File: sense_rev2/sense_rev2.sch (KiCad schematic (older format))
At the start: 48 parts, among them P1 TST, P2 TST, P3 TST, P4 TST, Q1 TSM2301, U1 PIR, U2 TLV8801, U3 TLV8801, U4 TPS61098, U5 hackaBLE_half, U6 TPS70630

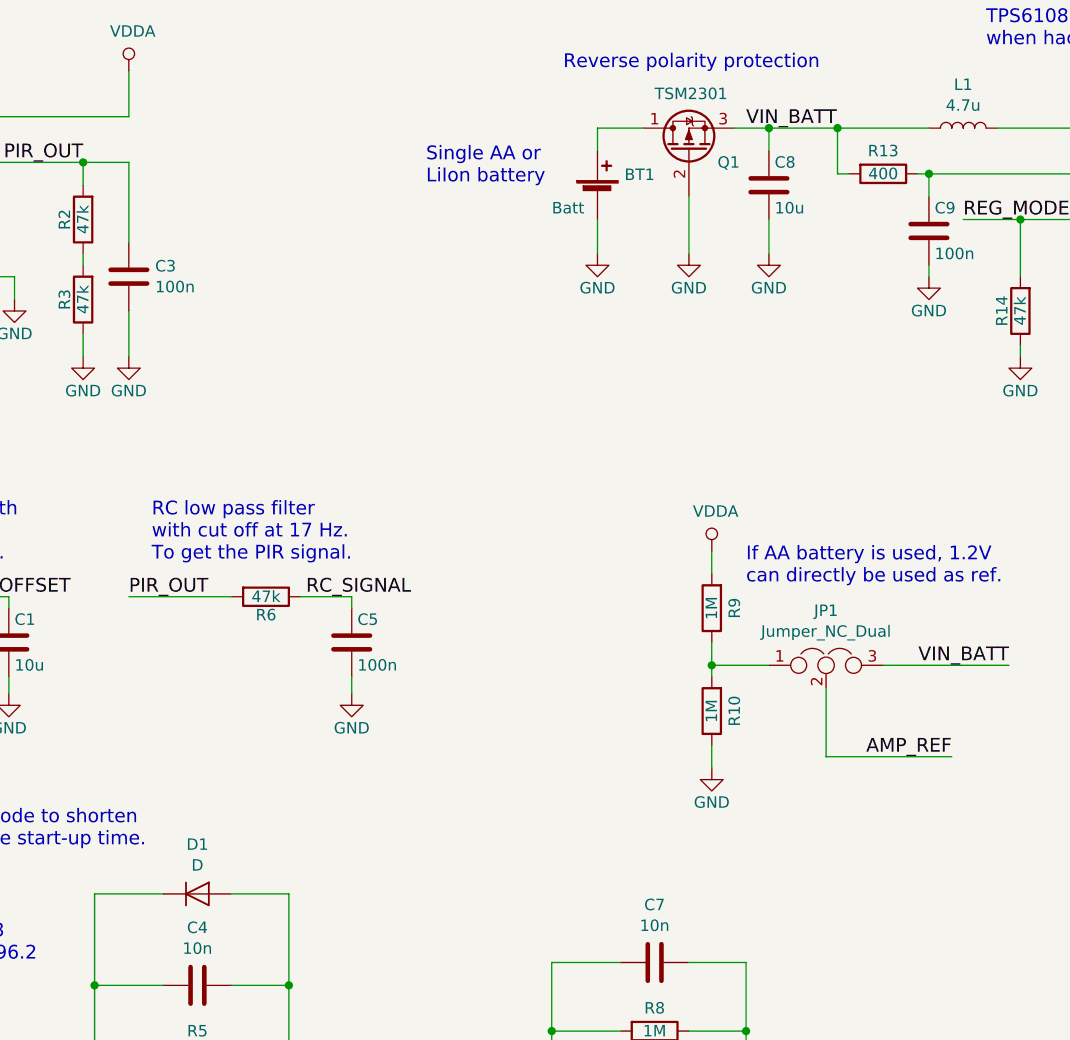
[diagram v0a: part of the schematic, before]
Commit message: Adds the datasheets the the symbols
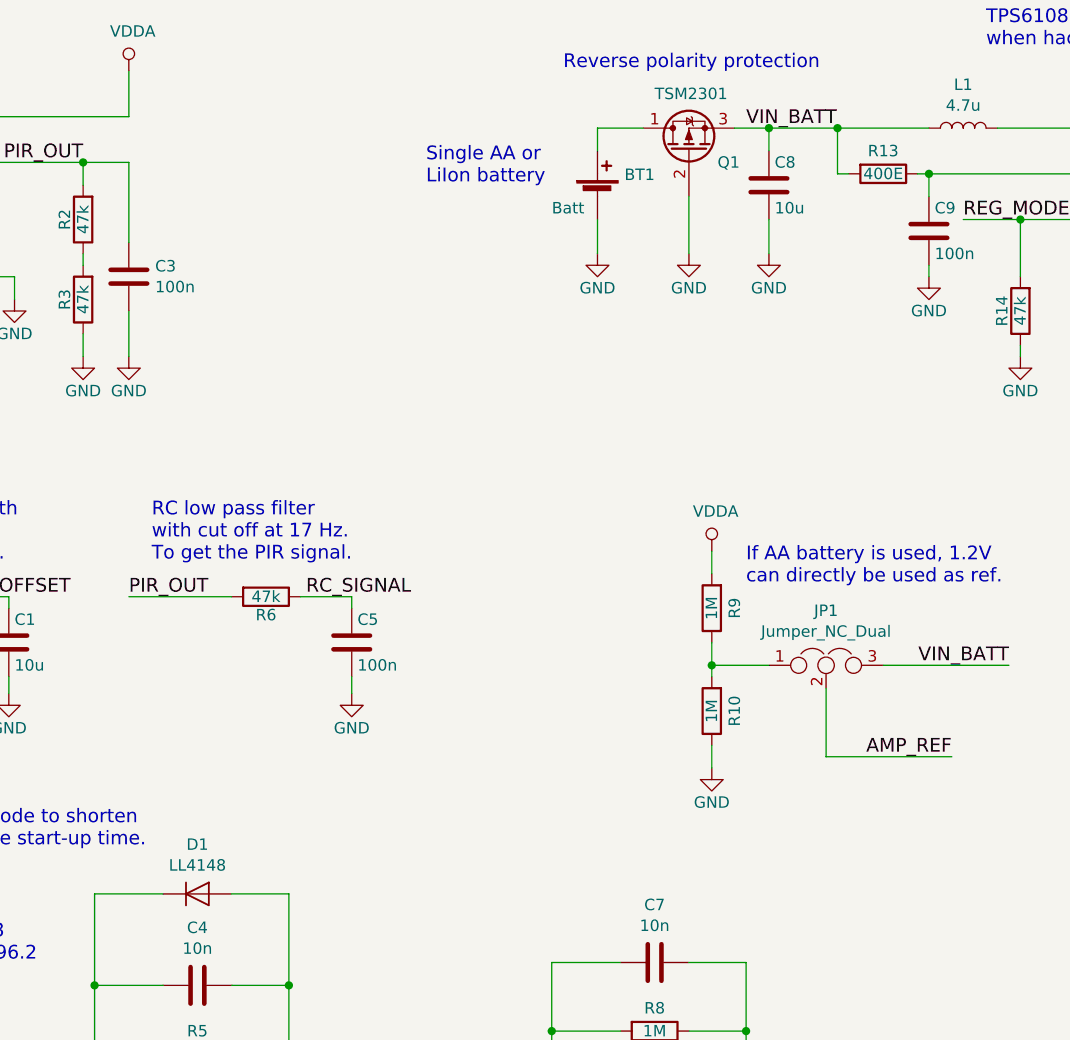
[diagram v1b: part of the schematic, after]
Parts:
- D1: value D -> LL4148
- R13: value 400 -> 400E
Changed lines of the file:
@@
 LIBS:contrib
 LIBS:hackable
-LIBS:pir_sensor
 LIBS:tps61098
 LIBS:sense_rev2-cache
@@
 P 2900 4700
 F 0 "D1" H 2900 4916 50  0000 C CNN
-F 1 "D" H 2900 4825 50  0000 C CNN
+F 1 "LL4148" H 2900 4825 50  0000 C CNN
 F 2 "Diodes_SMD:D_1206" H 2900 4700 50  0001 C CNN
-F 3 "" H 2900 4700 50  0001 C CNN
+F 3 "https://www.fairchildsemi.com/datasheets/LL/LL4148.pdf" H 2900 4700 50  0001 C CNN
 	1    2900 4700
 	1    0    0    -1
@@
 F 1 "TPS61098" H 7150 1926 50  0000 C CNN
 F 2 "Housings_SON:WSON6_1.5x1.5mm_Pitch0.5mm" H 7150 1975 50  0001 C CIN
-F 3 "" H 7100 1650 50  0001 C CNN
+F 3 "http://www.ti.com/lit/ds/symlink/tps610985.pdf" H 7100 1650 50  0001 C CNN
 	1    7150 1550
 	1    0    0    -1
@@
 P 5900 1550
 F 0 "R13" V 5800 1550 50  0000 C CNN
-F 1 "400" V 5900 1550 50  0000 C CNN
+F 1 "400E" V 5900 1550 50  0000 C CNN
 F 2 "Capacitors_SMD:C_0805" V 5830 1550 50  0001 C CNN
 F 3 "" H 5900 1550 50  0001 C CNN
@@
 F 1 "TPS70630" H 10000 1751 50  0000 C CNN
 F 2 "TO_SOT_Packages_SMD:SOT-23-5" H 10000 1825 50  0001 C CIN
-F 3 "" H 10000 1500 50  0001 C CNN
+F 3 "http://www.ti.com/lit/ds/symlink/tps706.pdf" H 10000 1500 50  0001 C CNN
 	1    10000 1500
 	1    0    0    -1
@@
 F 1 "hackaBLE_half" H 7850 3300 60  0000 C CNN
 F 2 "detect_trigger:hackable_footprint_half" H 7700 4050 60  0001 C CNN
-F 3 "" H 7700 4050 60  0001 C CNN
+F 3 "https://github.com/electronut/ElectronutLabs-hackaBLE" H 7700 4050 60  0001 C CNN
 	1    8200 4000
 	1    0    0    -1
